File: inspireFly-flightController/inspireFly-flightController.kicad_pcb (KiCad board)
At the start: 4 copper layers, 95.6 x 80 mm, 34 parts, among them J1 FTSH-107-01-L-DV-K-A, SW1 SW_Push, SW3 SW_Push, U1 STM32U595VJT6, U2 BNO086, Y1 ABS07-32.768KHZ-T, Y2 ABS07-32.768KHZ-T

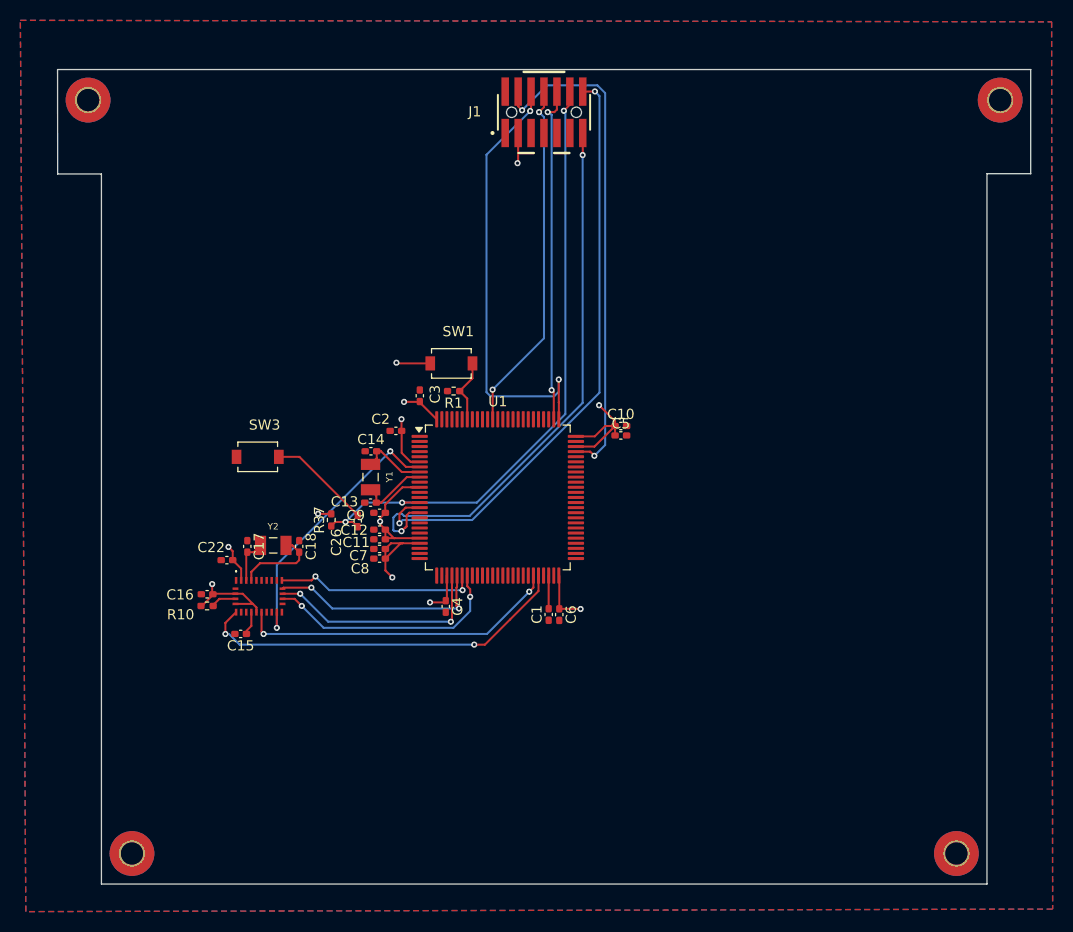
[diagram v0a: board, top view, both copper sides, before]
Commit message: RTC backup layout: placement and routing, setups A and B
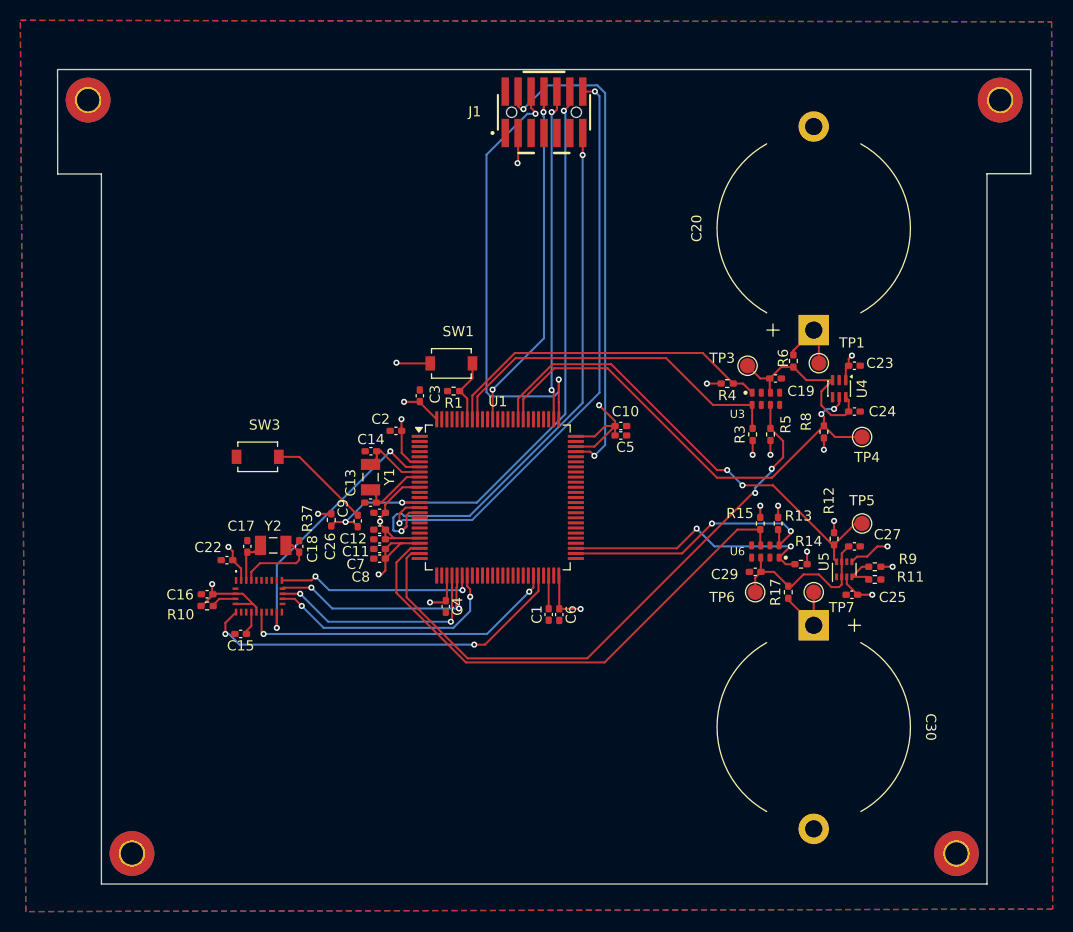
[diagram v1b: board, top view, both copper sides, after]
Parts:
- added C19: 10nF, Capacitor_SMD:C_0402_1005Metric_Pad0.74x0.62mm_HandSolder, F.Cu at (151.0, 69.5)
- added C20: 1.5F, inspirefly:SUPERCAP_KR-5R5H155-R, F.Cu at (154.8, 54.8)
- added C23: 1uF, Capacitor_SMD:C_0402_1005Metric_Pad0.74x0.62mm_HandSolder, F.Cu at (158.8, 68.2)
- added C24: 1uF, Capacitor_SMD:C_0402_1005Metric_Pad0.74x0.62mm_HandSolder, F.Cu at (158.8, 72.8)
- added C25: 1uF, Capacitor_SMD:C_0402_1005Metric_Pad0.74x0.62mm_HandSolder, F.Cu at (158.5, 90.8)
- added C27: 1uF, Capacitor_SMD:C_0402_1005Metric_Pad0.74x0.62mm_HandSolder, F.Cu at (158.8, 86.0)
- added C29: 10nF, Capacitor_SMD:C_0402_1005Metric_Pad0.74x0.62mm_HandSolder, F.Cu at (149.0, 88.5)
- added C30: 1.5F, inspirefly:SUPERCAP_KR-5R5H155-R, F.Cu at (154.8, 103.8)
- added R11: 100k, Resistor_SMD:R_0402_1005Metric_Pad0.72x0.64mm_HandSolder, F.Cu at (160.8, 89.2)
- added R12: 100k, Resistor_SMD:R_0402_1005Metric_Pad0.72x0.64mm_HandSolder, F.Cu at (156.8, 85.2)
- added R13: 10k, Resistor_SMD:R_0402_1005Metric_Pad0.72x0.64mm_HandSolder, F.Cu at (151.2, 83.8)
- added R14: 10k, Resistor_SMD:R_0402_1005Metric_Pad0.72x0.64mm_HandSolder, F.Cu at (153.5, 87.8)
- added R15: 10k, Resistor_SMD:R_0402_1005Metric_Pad0.72x0.64mm_HandSolder, F.Cu at (149.5, 83.8)
- added R17: 4.7k, Resistor_SMD:R_0402_1005Metric_Pad0.72x0.64mm_HandSolder, F.Cu at (152.2, 90.5)
- added R3: 10k, Resistor_SMD:R_0402_1005Metric_Pad0.72x0.64mm_HandSolder, F.Cu at (148.8, 75.0)
- added R4: 10k, Resistor_SMD:R_0402_1005Metric_Pad0.72x0.64mm_HandSolder, F.Cu at (146.2, 70.0)
- added R5: 10k, Resistor_SMD:R_0402_1005Metric_Pad0.72x0.64mm_HandSolder, F.Cu at (150.5, 75.0)
- added R6: 4.7k, Resistor_SMD:R_0402_1005Metric_Pad0.72x0.64mm_HandSolder, F.Cu at (152.8, 67.8)
- added R8: 100k, Resistor_SMD:R_0402_1005Metric_Pad0.72x0.64mm_HandSolder, F.Cu at (155.8, 74.8)
- added R9: 150k, Resistor_SMD:R_0402_1005Metric_Pad0.72x0.64mm_HandSolder, F.Cu at (160.8, 88.0)
- added TP1: VCAP_A1, TestPoint:TestPoint_Pad_D1.5mm, F.Cu at (155.2, 68.0)
- added TP3: VRTC_A, TestPoint:TestPoint_Pad_D1.5mm, F.Cu at (148.2, 68.2)
- added TP4: RTC_A_ST, TestPoint:TestPoint_Pad_D1.5mm, F.Cu at (159.5, 75.2)
- added TP5: RTC_B_ST, TestPoint:TestPoint_Pad_D1.5mm, F.Cu at (159.5, 83.8)
- added TP6: VRTC_B, TestPoint:TestPoint_Pad_D1.5mm, F.Cu at (149.0, 90.5)
- added TP7: VCAP_B1, TestPoint:TestPoint_Pad_D1.5mm, F.Cu at (154.8, 90.5)
- added U3: RV-8803-C7, inspirefly:RTC_RV-8803-C7, F.Cu at (150.1, 71.5)
- added U4: LM66100DCK, Package_TO_SOT_SMD:SOT-363_SC-70-6, F.Cu at (157.2, 70.5)
- added U5: TPS2117, inspirefly:PWRMUX_TPS2117-DRL, F.Cu at (157.8, 88.2)
- added U6: RV-8803-C7, inspirefly:RTC_RV-8803-C7, F.Cu at (150.0, 86.5)
- J1: footprint flightController:SAMTEC_FTSH-107-01-L-DV-K-A -> inspirefly:SAMTEC_FTSH-107-01-L-DV-K-A
- Y1, Y2: footprint flightController:XTAL_ABS07-32.768KHZ-T -> inspirefly:XTAL_ABS07-32.768KHZ-T
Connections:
- U1 pad 23: unconnected-(U1-PA0-Pad23) -> RTC_B_INT
- U1 pad 24: unconnected-(U1-PA1-Pad24) -> RTC_A_INT
- U1 pad 52: unconnected-(U1-PB13-Pad52) -> RTC_B_SCL
- U1 pad 53: unconnected-(U1-PB14-Pad53) -> RTC_B_SDA
- U1 pad 83: unconnected-(U1-PD2-Pad83) -> RTC_A_PWR_ST
- U1 pad 84: unconnected-(U1-PD3-Pad84) -> RTC_B_PWR_ST
- U1 pad 92: unconnected-(U1-PB6-Pad92) -> RTC_A_SCL
- U1 pad 93: unconnected-(U1-PB7-Pad93) -> RTC_A_SDA
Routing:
- net RTC_A_INT: track 0.00 -> 59.1 mm, vias 0 -> 2
- net RTC_B_INT: track 0.00 -> 51.4 mm
- net RTC_A_PWR_ST: track 0.00 -> 47.6 mm, vias 0 -> 2
- net RTC_B_PWR_ST: track 0.00 -> 47.2 mm, vias 0 -> 2
- net RTC_A_SCL: track 0.00 -> 35.0 mm
- net RTC_A_SDA: track 0.00 -> 33.2 mm
- net RTC_B_SCL: track 0.00 -> 26.1 mm, vias 0 -> 2
- net RTC_B_SDA: track 0.00 -> 26.1 mm, vias 0 -> 2
- net +3.3V: track 75.2 -> 96.8 mm, vias 12 -> 24
- net VRTC_A: track 0.00 -> 19.0 mm
- net VRTC_B: track 0.00 -> 17.3 mm
- net /VCAP_B1: track 0.00 -> 7.65 mm
- net /VCAP_A1: track 0.00 -> 6.72 mm
- net Net-(U5-PR1): track 0.00 -> 3.72 mm
- net JTCK/SWCLK: track 44.0 -> 44.7 mm
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
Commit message: added gnd vias for isolated island
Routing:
- net GND: track 0.00 -> 5.33 mm, vias 0 -> 3
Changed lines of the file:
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@@
+	)
+	(segment
+		(start 149.625 73.375)
+		(end 149.6 73.35)
+		(width 0.2)
+		(layer "F.Cu")
+		(net "GND")
+	)
+	(segment
+		(start 149.75 73.5)
+		(end 149.625 73.375)
+		(width 0.2)
+		(layer "F.Cu")
+		(net "GND")
+	)
+	(segment
+		(start 155.75 87.74)
+		(end 157 88.99)
+		(width 0.2)
+		(layer "F.Cu")
+		(net "GND")
+	)
+	(segment
+		(start 152 71.5)
+		(end 153.25 71.5)
+		(width 0.2)
+		(layer "F.Cu")
+		(net "GND")
+	)
+	(segment
+		(start 151.4 70.9)
+		(end 152 71.5)
+		(width 0.2)
+		(layer "F.Cu")
+		(net "GND")
+	)
+	(segment
+		(start 149.6 72.1)
+		(end 149.6 73.35)
+		(width 0.2)
+		(layer "F.Cu")
+		(net "GND")
+	)
+	(via
+		(at 153.25 71.5)
+		(size 0.6)
+		(drill 0.3)
+		(layers "F.Cu" "B.Cu")
+		(net "GND")
+	)
+	(via
+		(at 149.625 73.375)
+		(size 0.6)
+		(drill 0.3)
+		(layers "F.Cu" "B.Cu")
+		(net "GND")
+	)
+	(via
+		(at 155.75 87.74)
+		(size 0.6)
+		(drill 0.3)
+		(layers "F.Cu" "B.Cu")
+		(net "GND")
 	)
 	(segment
